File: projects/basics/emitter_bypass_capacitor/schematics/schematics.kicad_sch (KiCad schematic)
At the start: 7 parts, among them J1 5V, Q1 BC547

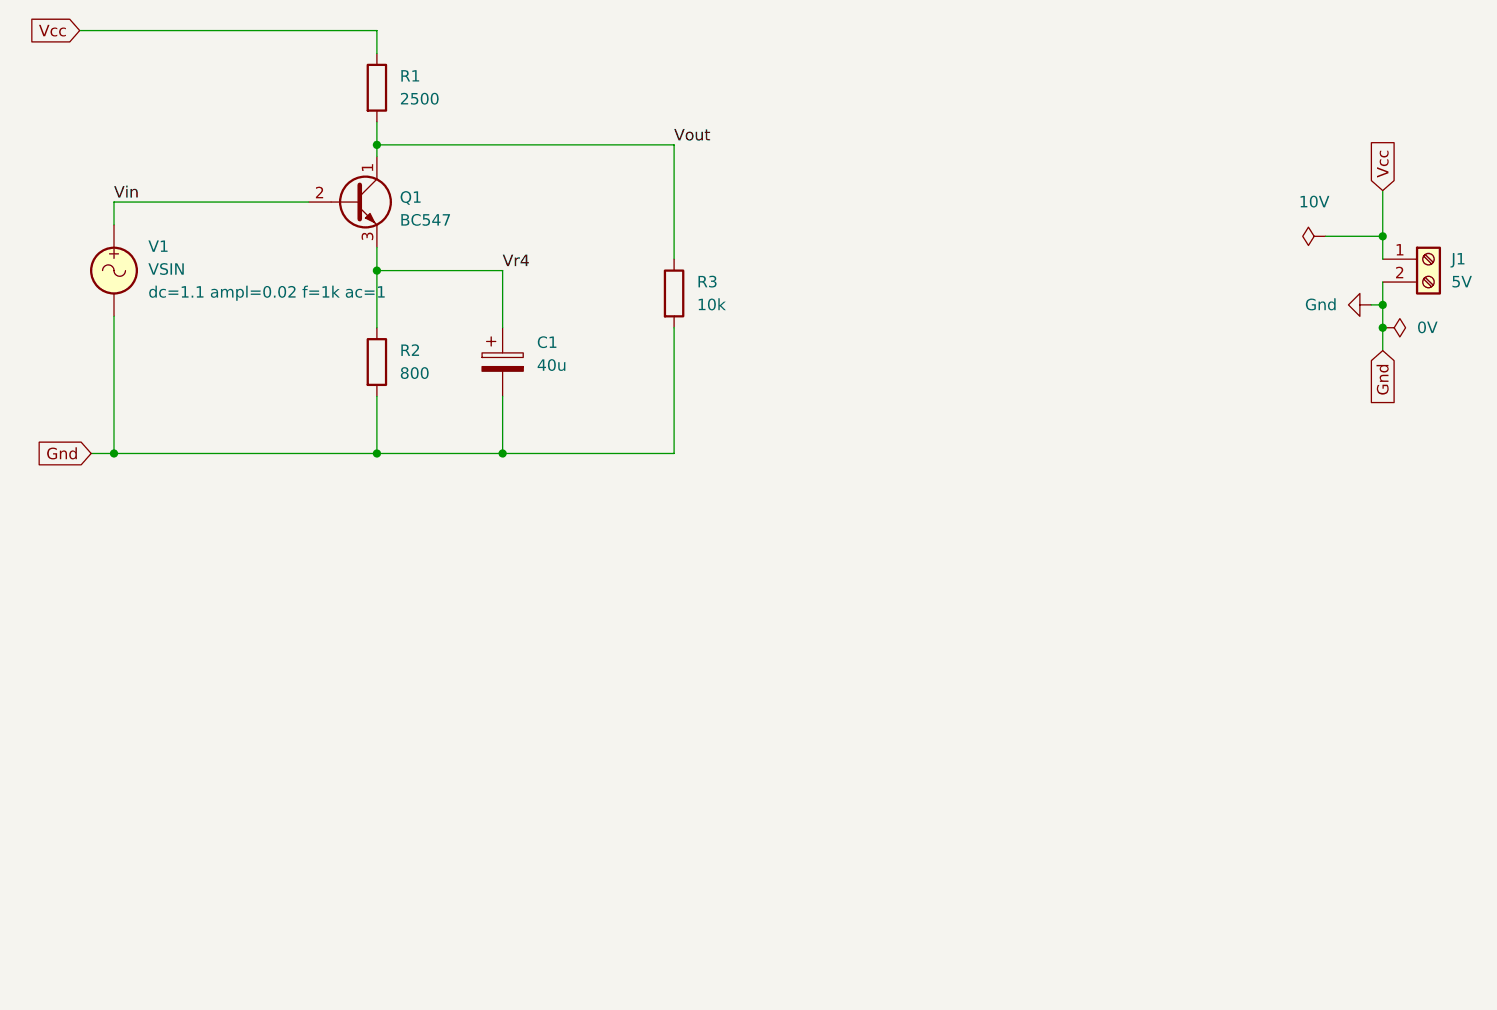
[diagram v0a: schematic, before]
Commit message: feat: Add practical and simulation images for emitter bypass capacitor project
Have completed multiple practical measurements and simulations to
illustrate the effects of varying emitter bypass capacitor values on
circuit performance.

Breaking changes: None

Resolves: None
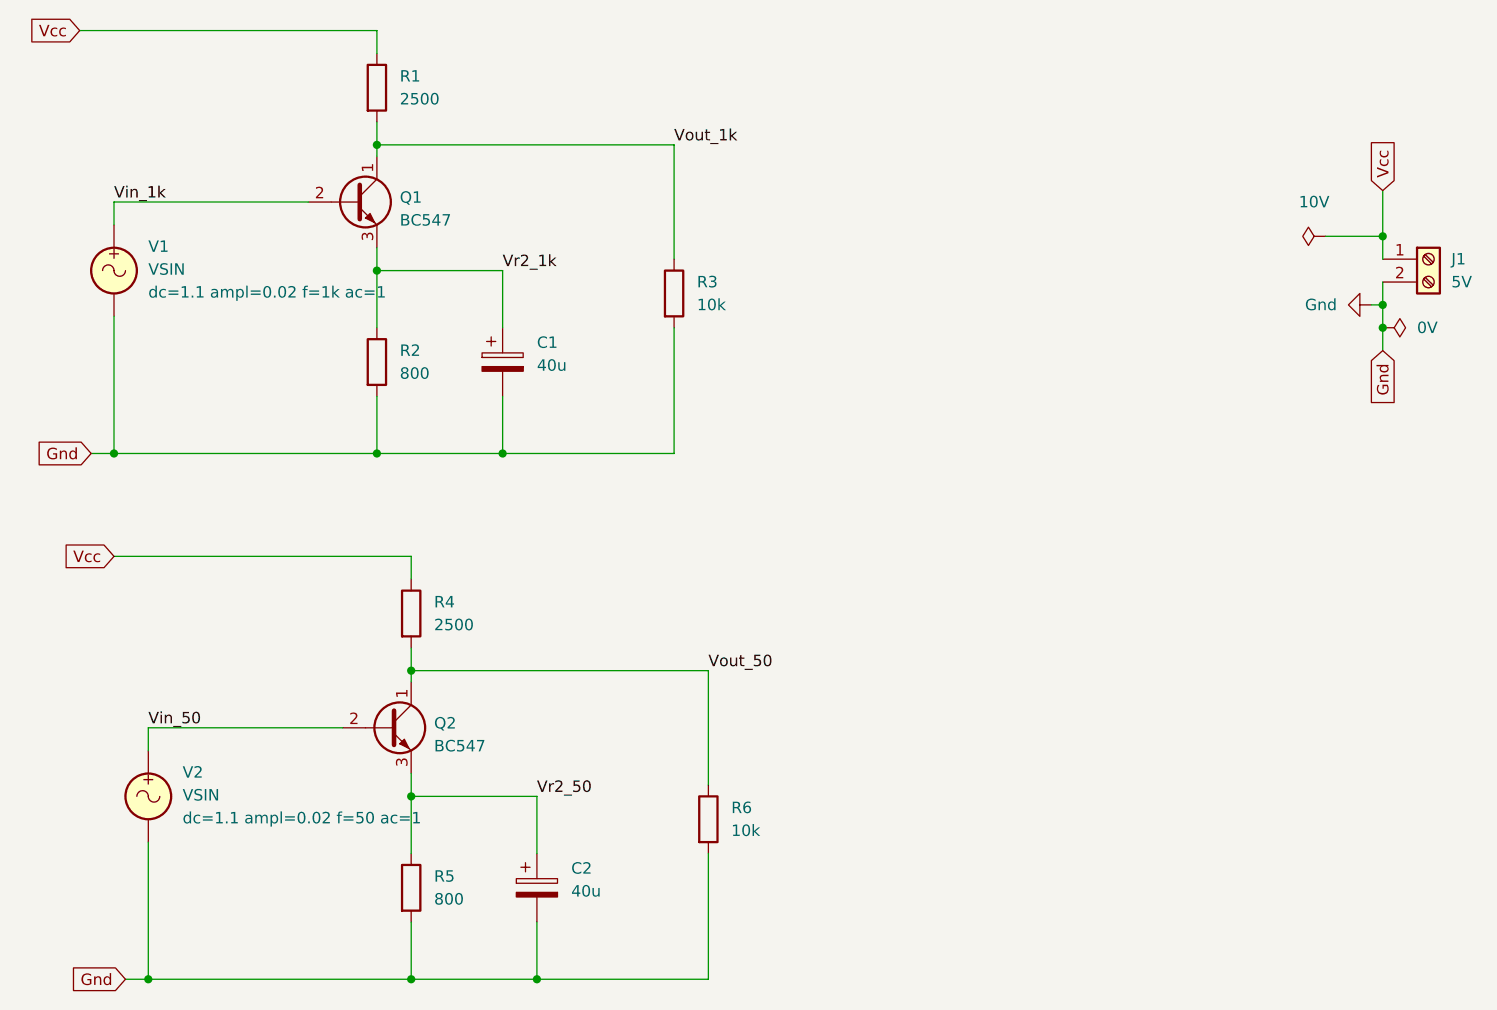
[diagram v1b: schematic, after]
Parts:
- added C2: 40u, symbol Device:C_Polarized
- added Q2: BC547, Package_TO_SOT_THT:TO-92_Inline, symbol Transistor_BJT:BC547
- added R4: 2500, symbol Device:R
- added R5: 800, symbol Device:R
- added R6: 10k, symbol Device:R
- added V2: VSIN, symbol Simulation_SPICE:VSIN
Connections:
- net Gnd: now also C2.2, R5.2, R6.2, V2.2
- net Vcc: now also R4.1
- net Vin renamed Vin_1k
- net Vout renamed Vout_1k
- net Vr4 renamed Vr2_1k
- new net Vin_50: Q2.2 (B), V2.1
- new net Vout_50: Q2.1 (C), R4.2, R6.1
- new net Vr2_50: C2.1, Q2.3 (E), R5.1

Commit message: feat: add emitter bypass capacitor high amplitude simulation and decoupling capacitor project
Added high amplitude simulation images to the emitter bypass capacitor project
to illustrate performance under different signal conditions.

Also introduced a new project on decoupling capacitors to enhance understanding
of their role in stabilizing voltage supply in electronic circuits.

Breaking changes: None

Resolves: None
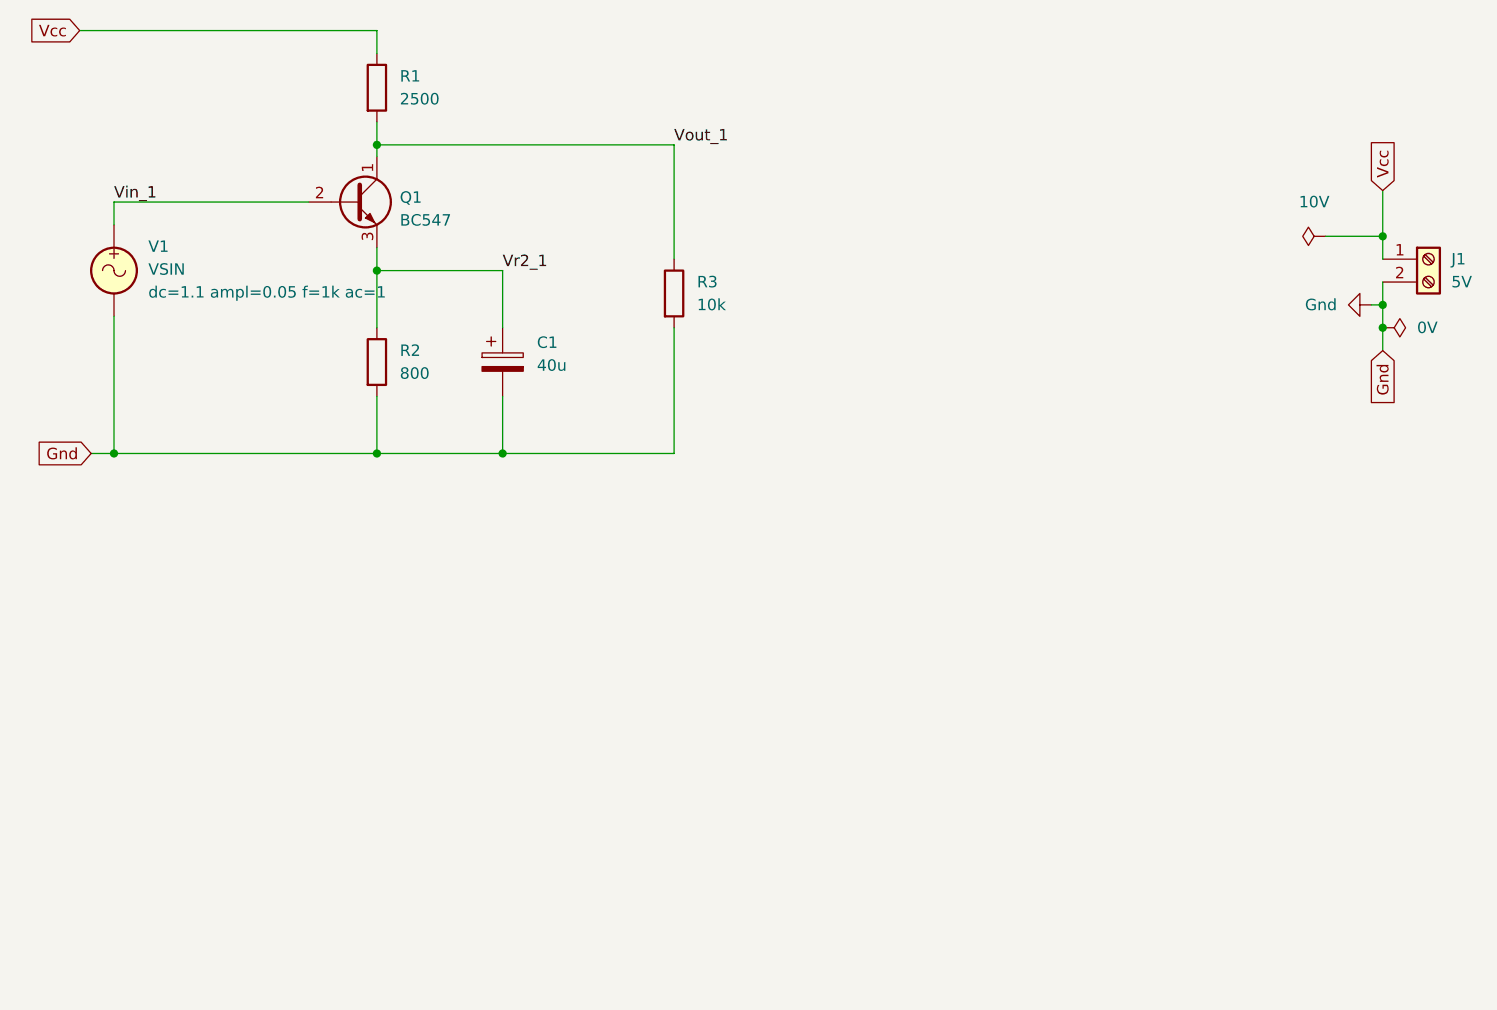
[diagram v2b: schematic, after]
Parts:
- removed C2: 40u, symbol Device:C_Polarized
- removed Q2: BC547, Package_TO_SOT_THT:TO-92_Inline, symbol Transistor_BJT:BC547
- removed R4: 2500, symbol Device:R
- removed R5: 800, symbol Device:R
- removed R6: 10k, symbol Device:R
- removed V2: VSIN, symbol Simulation_SPICE:VSIN
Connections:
- net Vin_1k renamed Vin_1
- net Vout_1k renamed Vout_1
- net Vr2_1k renamed Vr2_1

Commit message: feat: Completes emitter bypass capacitor project
Completes the emitter bypass capacitor project by adding practical
measurements for current for the ideal circuit. Also includes high
amplitude practical measurements.

Breaking changes: None

Resolves: None
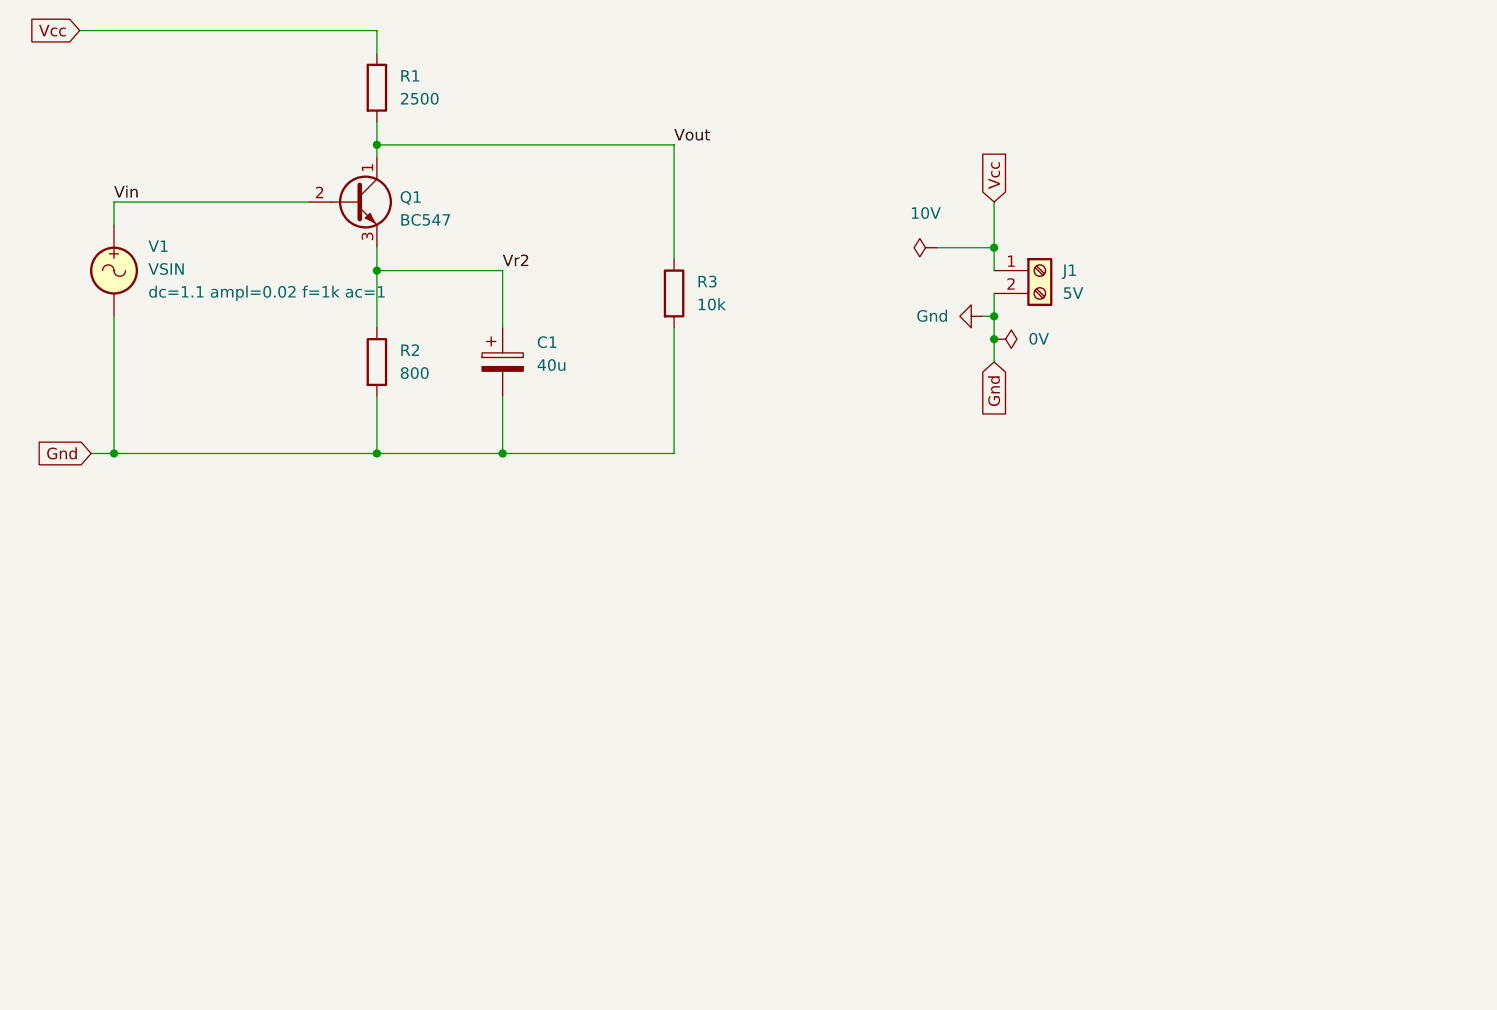
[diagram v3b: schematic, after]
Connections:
- net Vin_1 renamed Vin
- net Vout_1 renamed Vout
- net Vr2_1 renamed Vr2
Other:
- moved on the sheet: J1
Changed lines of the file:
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@@
 	(paper "A3")
 	(junction
-		(at 168.91 52.07)
+		(at 125.73 53.34)
 		(diameter 0)
 		(color 0 0 0 0)
@@
 	)
 	(junction
-		(at 168.91 54.61)
+		(at 125.73 55.88)
 		(diameter 0)
 		(color 0 0 0 0)
@@
 	)
 	(junction
-		(at 168.91 44.45)
+		(at 125.73 45.72)
 		(diameter 0)
 		(color 0 0 0 0)
@@
 	(wire
 		(pts
-			(xy 167.64 52.07) (xy 168.91 52.07)
-		)
-		(stroke
-			(width 0)
-			(type default)
-		)
-	)
-	(wire
-		(pts
-			(xy 168.91 46.99) (xy 168.91 44.45)
+			(xy 124.46 53.34) (xy 125.73 53.34)
+		)
+		(stroke
+			(width 0)
+			(type default)
+		)
+	)
+	(wire
+		(pts
+			(xy 125.73 48.26) (xy 125.73 45.72)
 		)
 		(stroke
@@
 	(wire
 		(pts
-			(xy 162.56 44.45) (xy 168.91 44.45)
+			(xy 119.38 45.72) (xy 125.73 45.72)
 		)
 		(stroke
@@
 	(wire
 		(pts
+			(xy 27.94 40.64) (xy 49.53 40.64)
+		)
+		(stroke
+			(width 0)
+			(type default)
+		)
+	)
+	(wire
+		(pts
 			(xy 57.15 68.58) (xy 57.15 62.23)
 		)
@@
 	(wire
 		(pts
-			(xy 168.91 39.37) (xy 168.91 44.45)
+			(xy 125.73 40.64) (xy 125.73 45.72)
 		)
 		(stroke
@@
 	(wire
 		(pts
-			(xy 27.94 40.64) (xy 49.53 40.64)
-		)
-		(stroke
-			(width 0)
-			(type default)
-		)
-	)
-	(wire
-		(pts
 			(xy 27.94 43.18) (xy 27.94 40.64)
 		)
@@
 	(wire
 		(pts
-			(xy 168.91 52.07) (xy 168.91 54.61)
-		)
-		(stroke
-			(width 0)
-			(type default)
-		)
-	)
-	(wire
-		(pts
-			(xy 168.91 49.53) (xy 168.91 52.07)
+			(xy 125.73 53.34) (xy 125.73 55.88)
+		)
+		(stroke
+			(width 0)
+			(type default)
+		)
+	)
+	(wire
+		(pts
+			(xy 125.73 50.8) (xy 125.73 53.34)
 		)
 		(stroke
@@
 	(wire
 		(pts
-			(xy 168.91 54.61) (xy 168.91 57.15)
+			(xy 125.73 55.88) (xy 125.73 58.42)
 		)
 		(stroke
@@
 		)
 	)
-	(label "Vout_1"
+	(label "Vout"
 		(at 90.17 34.29 0)
 		(effects
@@
 		)
 	)
-	(label "Vr2_1"
+	(label "Vr2"
 		(at 71.12 48.26 0)
 		(effects
@@
 		)
 	)
-	(label "Vin_1"
+	(label "Vin"
 		(at 27.94 40.64 0)
 		(effects
@@
 	(global_label "Gnd"
 		(shape input)
-		(at 168.91 57.15 270)
+		(at 125.73 58.42 270)
 		(fields_autoplaced yes)
 		(effects
@@
 		)
 		(property "Intersheetrefs" "${INTERSHEET_REFS}"
-			(at 168.91 63.7032 90)
+			(at 125.73 64.9732 90)
 			(effects
 				(font
@@
 	(global_label "Vcc"
 		(shape input)
-		(at 168.91 39.37 90)
+		(at 125.73 40.64 90)
 		(fields_autoplaced yes)
 		(effects
@@
 		)
 		(property "Intersheetrefs" "${INTERSHEET_REFS}"
-			(at 168.91 33.119 90)
+			(at 125.73 34.389 90)
 			(effects
 				(font
@@
 	(symbol
 		(lib_id "Connector:Screw_Terminal_01x02")
-		(at 173.99 46.99 0)
+		(at 130.81 48.26 0)
 		(unit 1)
 		(exclude_from_sim no)
@@
 		(fields_autoplaced yes)
 		(property "Reference" "J1"
-			(at 176.53 46.9899 0)
+			(at 133.35 48.2599 0)
 			(effects
 				(font
@@
 		)
 		(property "Value" "5V"
-			(at 176.53 49.5299 0)
+			(at 133.35 50.7999 0)
 			(effects
 				(font
@@
 		)
 		(property "Footprint" "TerminalBlock:TerminalBlock_Xinya_XY308-2.54-2P_1x02_P2.54mm_Horizontal"
-			(at 173.99 46.99 0)
+			(at 130.81 48.26 0)
 			(effects
 				(font
@@
 		)
 		(property "Datasheet" "~"
-			(at 173.99 46.99 0)
+			(at 130.81 48.26 0)
 			(effects
 				(font
@@
 		)
 		(property "Description" "Generic screw terminal, single row, 01x02, script generated (kicad-library-utils/schlib/autogen/connector/)"
-			(at 173.99 46.99 0)
+			(at 130.81 48.26 0)
 			(effects
 				(font
@@
 		)
 		(property "Sim.Device" "V"
-			(at 173.99 46.99 0)
+			(at 130.81 48.26 0)
 			(effects
 				(font
@@
 		)
 		(property "Sim.Type" "DC"
-			(at 173.99 46.99 0)
+			(at 130.81 48.26 0)
 			(effects
 				(font
@@
 		)
 		(property "Sim.Pins" "1=+ 2=-"
-			(at 173.99 46.99 0)
+			(at 130.81 48.26 0)
 			(effects
 				(font
@@
 	(symbol
 		(lib_id "power:PWR_FLAG")
-		(at 168.91 54.61 270)
+		(at 125.73 55.88 270)
 		(unit 1)
 		(exclude_from_sim no)
@@
 		(fields_autoplaced yes)
 		(property "Reference" "#FLG02"
-			(at 170.815 54.61 0)
+			(at 127.635 55.88 0)
 			(effects
 				(font
@@
 		)
 		(property "Value" "0V"
-			(at 172.72 54.6099 90)
+			(at 129.54 55.8799 90)
 			(effects
 				(font
@@
 		)
 		(property "Footprint" ""
-			(at 168.91 54.61 0)
+			(at 125.73 55.88 0)
 			(effects
 				(font
@@
 		)
 		(property "Datasheet" "~"
-			(at 168.91 54.61 0)
+			(at 125.73 55.88 0)
 			(effects
 				(font
@@
 		)
 		(property "Description" "Special symbol for telling ERC where power comes from"
-			(at 168.91 54.61 0)
+			(at 125.73 55.88 0)
 			(effects
 				(font
@@
 			)
 		)
-		(property "Sim.Params" "dc=1.1 ampl=0.05 f=1k ac=1"
+		(property "Sim.Params" "dc=1.1 ampl=0.02 f=1k ac=1"
 			(at 31.75 50.6701 0)
 			(effects
@@
 	(symbol
 		(lib_id "power:PWR_FLAG")
-		(at 162.56 44.45 90)
+		(at 119.38 45.72 90)
 		(unit 1)
 		(exclude_from_sim no)
@@
 		(fields_autoplaced yes)
 		(property "Reference" "#FLG01"
-			(at 160.655 44.45 0)
+			(at 117.475 45.72 0)
 			(effects
 				(font
@@
 		)
 		(property "Value" "10V"
-			(at 161.29 40.64 90)
+			(at 118.11 41.91 90)
 			(effects
 				(font
@@
 		)
 		(property "Footprint" ""
-			(at 162.56 44.45 0)
+			(at 119.38 45.72 0)
 			(effects
 				(font
@@
 		)
 		(property "Datasheet" "~"
-			(at 162.56 44.45 0)
+			(at 119.38 45.72 0)
 			(effects
 				(font
@@
 		)
 		(property "Description" "Special symbol for telling ERC where power comes from"
-			(at 162.56 44.45 0)
+			(at 119.38 45.72 0)
 			(effects
 				(font
@@
 	(symbol
 		(lib_id "power:GND")
-		(at 167.64 52.07 270)
+		(at 124.46 53.34 270)
 		(unit 1)
 		(exclude_from_sim no)
@@
 		(fields_autoplaced yes)
 		(property "Reference" "#PWR01"
-			(at 161.29 52.07 0)
+			(at 118.11 53.34 0)
 			(effects
 				(font
@@
 		)
 		(property "Value" "Gnd"
-			(at 163.83 52.0699 90)
+			(at 120.65 53.3399 90)
 			(effects
 				(font
@@
 		)
 		(property "Footprint" ""
-			(at 167.64 52.07 0)
+			(at 124.46 53.34 0)
 			(effects
 				(font
@@
 		)
 		(property "Datasheet" ""
-			(at 167.64 52.07 0)
+			(at 124.46 53.34 0)
 			(effects
 				(font
@@
 		)
 		(property "Description" "Power symbol creates a global label with name \"GND\" , ground"
-			(at 167.64 52.07 0)
-			(effects
-				(font
+			(at 124.46 53.34 0)
+			(effects
+				(font
